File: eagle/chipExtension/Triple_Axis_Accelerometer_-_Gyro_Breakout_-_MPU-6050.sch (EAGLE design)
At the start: 17 parts, among them U1 MPU-6050-1, U3 PCA9685

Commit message: Adding holes to the PCB on eagle and enhancing the freeca model of cylinder prototype 3.
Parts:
- added JP2, JP3, JP4, JP5, JP6, JP7, JP8, JP9: (no value), jumper:JP4E
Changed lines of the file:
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@@
 <part name="P+5" library="supply1" library_urn="urn:adsk.eagle:library:371" deviceset="VCC" device=""/>
 <part name="P+6" library="supply1" library_urn="urn:adsk.eagle:library:371" deviceset="VCC" device=""/>
+<part name="JP2" library="jumper" library_urn="urn:adsk.eagle:library:252" deviceset="JP4E" device=""/>
+<part name="JP3" library="jumper" library_urn="urn:adsk.eagle:library:252" deviceset="JP4E" device=""/>
+<part name="JP4" library="jumper" library_urn="urn:adsk.eagle:library:252" deviceset="JP4E" device=""/>
+<part name="JP5" library="jumper" library_urn="urn:adsk.eagle:library:252" deviceset="JP4E" device=""/>
+<part name="JP6" library="jumper" library_urn="urn:adsk.eagle:library:252" deviceset="JP4E" device=""/>
+<part name="JP7" library="jumper" library_urn="urn:adsk.eagle:library:252" deviceset="JP4E" device=""/>
+<part name="JP8" library="jumper" library_urn="urn:adsk.eagle:library:252" deviceset="JP4E" device=""/>
+<part name="JP9" library="jumper" library_urn="urn:adsk.eagle:library:252" deviceset="JP4E" device=""/>
 </parts>
 <sheets>
@@
 <instance part="P+5" gate="VCC" x="40.64" y="20.32"/>
 <instance part="P+6" gate="VCC" x="40.64" y="10.16"/>
+<instance part="JP2" gate="G$1" x="-177.8" y="93.98" rot="R90"/>
+<instance part="JP3" gate="G$1" x="-177.8" y="76.2" rot="R90"/>
+<instance part="JP4" gate="G$1" x="-177.8" y="55.88" rot="R90"/>
+<instance part="JP5" gate="G$1" x="-177.8" y="35.56" rot="R90"/>
+<instance part="JP6" gate="G$1" x="-193.04" y="96.52" rot="R270"/>
+<instance part="JP7" gate="G$1" x="-193.04" y="78.74" rot="R270"/>
+<instance part="JP8" gate="G$1" x="-193.04" y="58.42" rot="R270"/>
+<instance part="JP9" gate="G$1" x="-193.04" y="38.1" rot="R270"/>
 </instances>
 <busses>

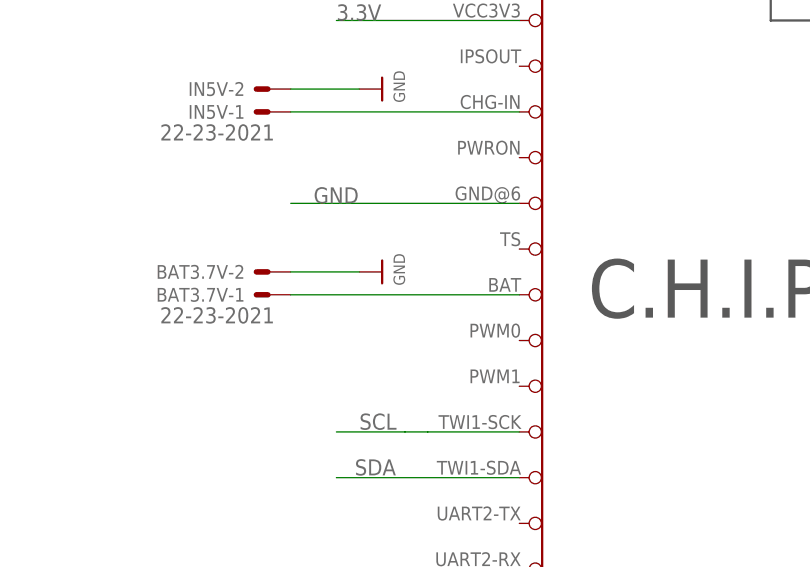
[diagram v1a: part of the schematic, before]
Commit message: Adding jumper to eagle files and enhancing the freecad model of cylinderPrototype3.
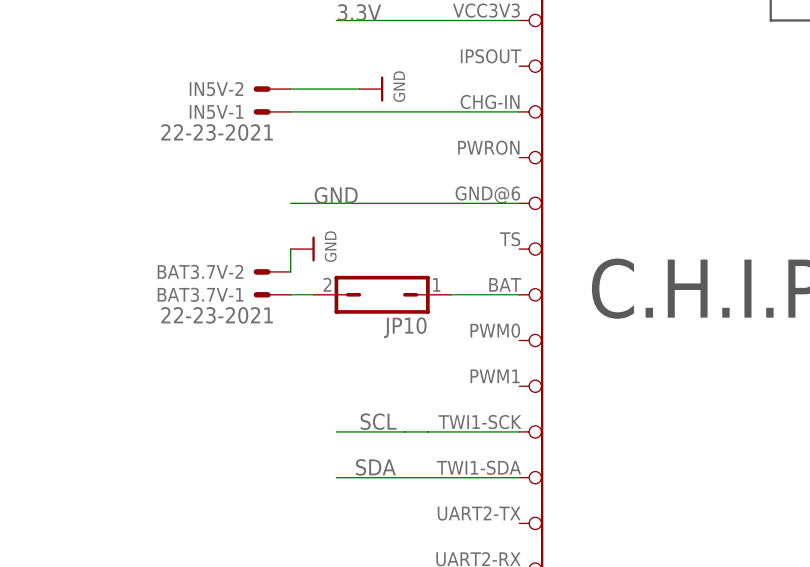
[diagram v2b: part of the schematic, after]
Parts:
- added JP10: (no value), jumper:JP1Q
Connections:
- net VCC: now also JP10.1, JP10.2
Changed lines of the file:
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@@
 <part name="JP8" library="jumper" library_urn="urn:adsk.eagle:library:252" deviceset="JP4E" device=""/>
 <part name="JP9" library="jumper" library_urn="urn:adsk.eagle:library:252" deviceset="JP4E" device=""/>
+<part name="JP10" library="jumper" library_urn="urn:adsk.eagle:library:252" deviceset="JP1Q" device=""/>
 </parts>
 <sheets>
@@
 <instance part="BAT3.7V" gate="-2" x="-144.78" y="71.12" rot="R180"/>
 <instance part="U$2" gate="G$1" x="-132.08" y="91.44" rot="R90"/>
-<instance part="U$3" gate="G$1" x="-132.08" y="71.12" rot="R90"/>
+<instance part="U$3" gate="G$1" x="-139.7" y="73.66" rot="R90"/>
 <instance part="P+3" gate="VCC" x="40.64" y="40.64"/>
 <instance part="P+4" gate="VCC" x="40.64" y="30.48"/>
@@
 <instance part="JP8" gate="G$1" x="-193.04" y="58.42" rot="R270"/>
 <instance part="JP9" gate="G$1" x="-193.04" y="38.1" rot="R270"/>
+<instance part="JP10" gate="A" x="-132.08" y="68.58" rot="R90"/>
 </instances>
 <busses>
@@
 <segment>
 <pinref part="U$1" gate="G$1" pin="BAT"/>
-<pinref part="BAT3.7V" gate="-1" pin="S"/>
-<wire x1="-142.24" y1="68.58" x2="-116.84" y2="68.58" width="0.1524" layer="91"/>
+<pinref part="JP10" gate="A" pin="1"/>
+<wire x1="-124.46" y1="68.58" x2="-116.84" y2="68.58" width="0.1524" layer="91"/>
 </segment>
 <segment>
@@
 <pinref part="JP1" gate="G$1" pin="11"/>
 <pinref part="P+6" gate="VCC" pin="VCC"/>
+</segment>
+<segment>
+<pinref part="BAT3.7V" gate="-1" pin="S"/>
+<wire x1="-142.24" y1="68.58" x2="-139.7" y2="68.58" width="0.1524" layer="91"/>
+<pinref part="JP10" gate="A" pin="2"/>
 </segment>
 </net>
@@
 <segment>
 <pinref part="BAT3.7V" gate="-2" pin="S"/>
-<wire x1="-142.24" y1="71.12" x2="-134.62" y2="71.12" width="0.1524" layer="91"/>
+<wire x1="-142.24" y1="71.12" x2="-142.24" y2="73.66" width="0.1524" layer="91"/>
 <pinref part="U$3" gate="G$1" pin="GND"/>
 </segment>

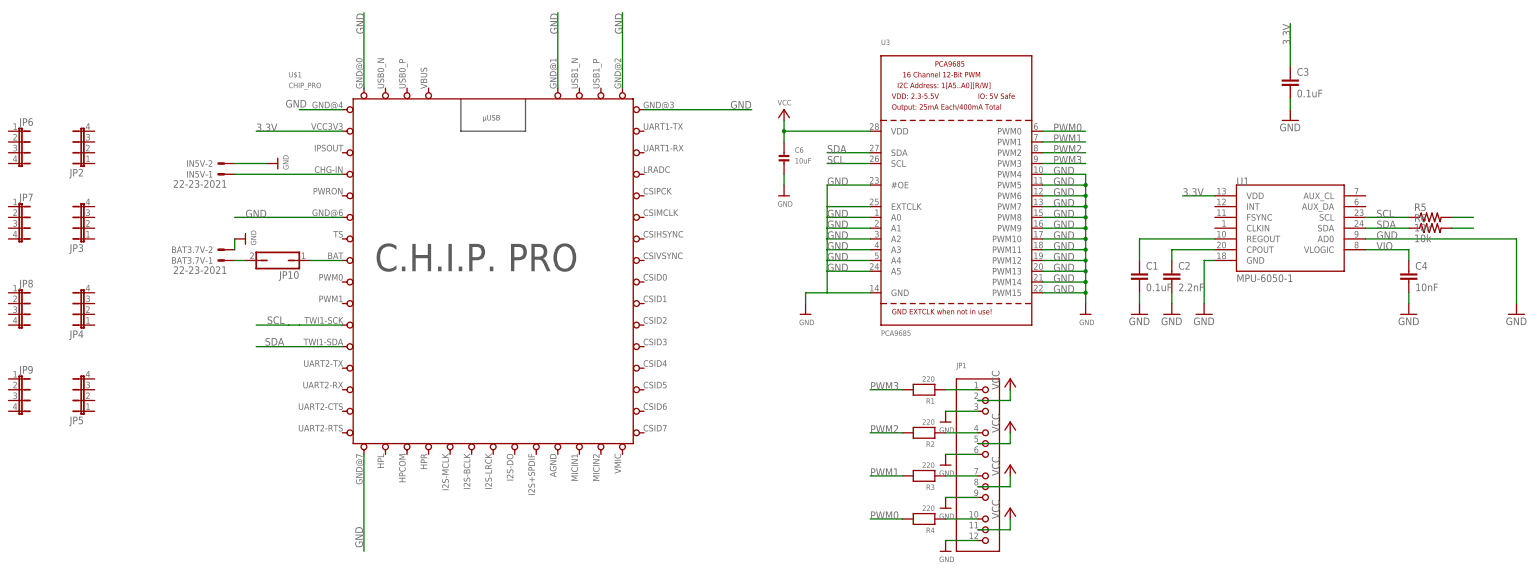
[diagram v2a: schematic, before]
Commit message: improve eagle design
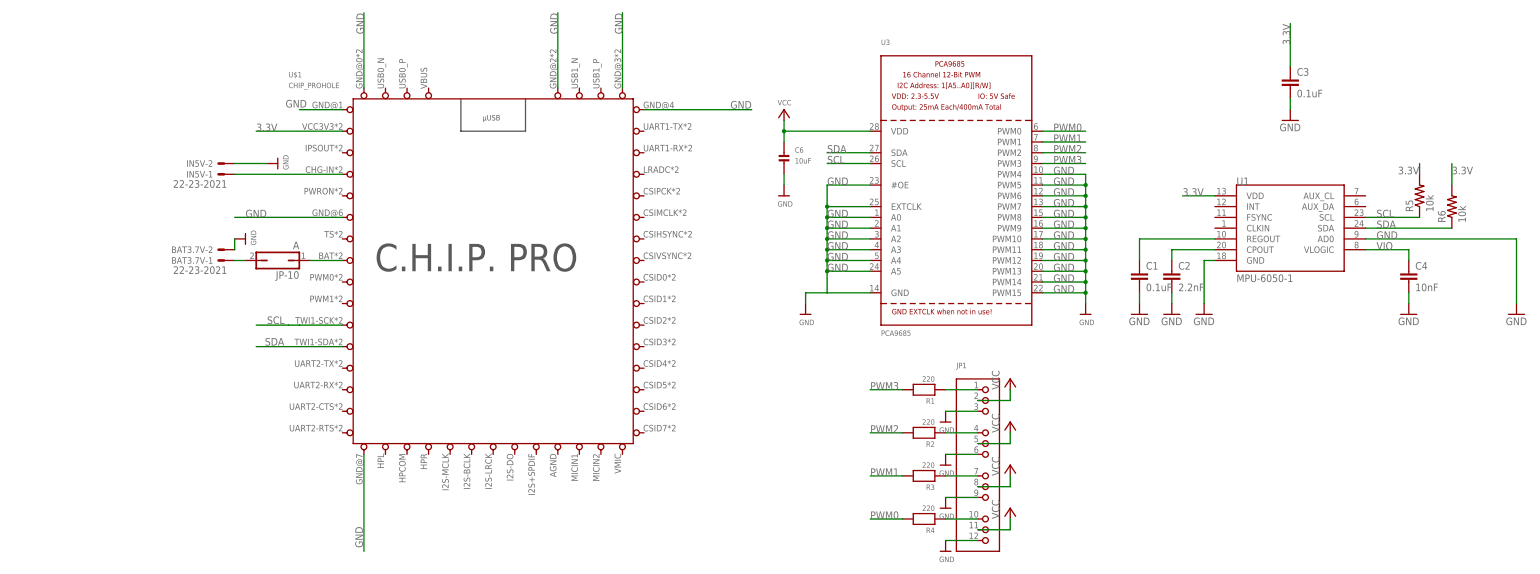
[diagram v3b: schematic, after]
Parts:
- removed JP2, JP3, JP4, JP5, JP6, JP7, JP8, JP9: (no value), jumper:JP4E
- JP-10: value (none) -> A
- U$1: value CHIP_PRO -> CHIP_PROHOLE; device CHIP_Pro-Footprint:CHIP_PRO -> CHIP_Pro-Footprint:CHIP_PROHOLE
- renumbered JP10 to JP-10
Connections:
- net 3.3V: now also R5.2, R6.2
- net SCL: no longer R5.2
- net SDA: no longer R6.2
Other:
- moved on the sheet: R5, R6, U$1
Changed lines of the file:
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@@
 <part name="R4" library="microbuilder" deviceset="RESISTOR" device="0805" value="220"/>
 <part name="JP1" library="microbuilder" deviceset="HEADER-3X04" device=""/>
-<part name="U$1" library="CHIP_Pro-Footprint" deviceset="CHIP_PRO" device=""/>
+<part name="U$1" library="CHIP_Pro-Footprint" deviceset="CHIP_PRO" device="HOLE" value="CHIP_PROHOLE"/>
 <part name="U$9" library="microbuilder" deviceset="GND" device=""/>
 <part name="R5" library="rcl" library_urn="urn:adsk.eagle:library:334" deviceset="R-US_" device="R0805" value="10k"/>
@@
 <part name="P+5" library="supply1" library_urn="urn:adsk.eagle:library:371" deviceset="VCC" device=""/>
 <part name="P+6" library="supply1" library_urn="urn:adsk.eagle:library:371" deviceset="VCC" device=""/>
-<part name="JP2" library="jumper" library_urn="urn:adsk.eagle:library:252" deviceset="JP4E" device=""/>
-<part name="JP3" library="jumper" library_urn="urn:adsk.eagle:library:252" deviceset="JP4E" device=""/>
-<part name="JP4" library="jumper" library_urn="urn:adsk.eagle:library:252" deviceset="JP4E" device=""/>
-<part name="JP5" library="jumper" library_urn="urn:adsk.eagle:library:252" deviceset="JP4E" device=""/>
-<part name="JP6" library="jumper" library_urn="urn:adsk.eagle:library:252" deviceset="JP4E" device=""/>
-<part name="JP7" library="jumper" library_urn="urn:adsk.eagle:library:252" deviceset="JP4E" device=""/>
-<part name="JP8" library="jumper" library_urn="urn:adsk.eagle:library:252" deviceset="JP4E" device=""/>
-<part name="JP9" library="jumper" library_urn="urn:adsk.eagle:library:252" deviceset="JP4E" device=""/>
-<part name="JP10" library="jumper" library_urn="urn:adsk.eagle:library:252" deviceset="JP1Q" device=""/>
+<part name="JP-10" library="jumper" library_urn="urn:adsk.eagle:library:252" deviceset="JP1Q" device="" value="A"/>
 </parts>
 <sheets>
@@
 <instance part="U$1" gate="G$1" x="-81.28" y="63.5"/>
 <instance part="U$9" gate="G$1" x="58.42" y="55.88"/>
-<instance part="R5" gate="G$1" x="139.7" y="78.74"/>
-<instance part="R6" gate="G$1" x="139.7" y="76.2"/>
+<instance part="R5" gate="G$1" x="137.16" y="83.82" rot="R90"/>
+<instance part="R6" gate="G$1" x="144.78" y="81.28" rot="R90"/>
 <instance part="IN5V" gate="-1" x="-144.78" y="88.9" rot="R180"/>
 <instance part="IN5V" gate="-2" x="-144.78" y="91.44" rot="R180"/>
@@
 <instance part="P+5" gate="VCC" x="40.64" y="20.32"/>
 <instance part="P+6" gate="VCC" x="40.64" y="10.16"/>
-<instance part="JP2" gate="G$1" x="-177.8" y="93.98" rot="R90"/>
-<instance part="JP3" gate="G$1" x="-177.8" y="76.2" rot="R90"/>
-<instance part="JP4" gate="G$1" x="-177.8" y="55.88" rot="R90"/>
-<instance part="JP5" gate="G$1" x="-177.8" y="35.56" rot="R90"/>
-<instance part="JP6" gate="G$1" x="-193.04" y="96.52" rot="R270"/>
-<instance part="JP7" gate="G$1" x="-193.04" y="78.74" rot="R270"/>
-<instance part="JP8" gate="G$1" x="-193.04" y="58.42" rot="R270"/>
-<instance part="JP9" gate="G$1" x="-193.04" y="38.1" rot="R270"/>
-<instance part="JP10" gate="A" x="-132.08" y="68.58" rot="R90"/>
+<instance part="JP-10" gate="A" x="-132.08" y="68.58" rot="R90"/>
 </instances>
 <busses>
@@
 <segment>
 <pinref part="U$1" gate="G$1" pin="BAT"/>
-<pinref part="JP10" gate="A" pin="1"/>
+<pinref part="JP-10" gate="A" pin="1"/>
 <wire x1="-124.46" y1="68.58" x2="-116.84" y2="68.58" width="0.1524" layer="91"/>
 </segment>
@@
 <pinref part="BAT3.7V" gate="-1" pin="S"/>
 <wire x1="-142.24" y1="68.58" x2="-139.7" y2="68.58" width="0.1524" layer="91"/>
-<pinref part="JP10" gate="A" pin="2"/>
+<pinref part="JP-10" gate="A" pin="2"/>
 </segment>
 </net>
@@
 <pinref part="U3" gate="G$1" pin="#OE"/>
 <wire x1="-2.54" y1="86.36" x2="-2.54" y2="81.28" width="0.1524" layer="91"/>
+<junction x="-2.54" y="81.28"/>
+<junction x="-2.54" y="78.74"/>
+<junction x="-2.54" y="76.2"/>
+<junction x="-2.54" y="73.66"/>
+<junction x="-2.54" y="71.12"/>
+<junction x="-2.54" y="68.58"/>
+<junction x="-2.54" y="66.04"/>
 </segment>
 <segment>
@@
 <pinref part="U1" gate="G$1" pin="SCL"/>
 <pinref part="R5" gate="G$1" pin="1"/>
-<wire x1="134.62" y1="78.74" x2="124.46" y2="78.74" width="0.1524" layer="91"/>
+<wire x1="137.16" y1="78.74" x2="124.46" y2="78.74" width="0.1524" layer="91"/>
 </segment>
 <segment>
@@
 <label x="-134.62" y="53.594" size="1.778" layer="95"/>
 </segment>
-<segment>
-<pinref part="R5" gate="G$1" pin="2"/>
-<wire x1="144.78" y1="78.74" x2="149.86" y2="78.74" width="0.1524" layer="91"/>
-</segment>
 </net>
 <net name="SDA" class="0">
@@
 <pinref part="U1" gate="G$1" pin="SDA"/>
 <pinref part="R6" gate="G$1" pin="1"/>
-<wire x1="134.62" y1="76.2" x2="124.46" y2="76.2" width="0.1524" layer="91"/>
+<wire x1="144.78" y1="76.2" x2="124.46" y2="76.2" width="0.1524" layer="91"/>
 </segment>
 <segment>
@@
 <wire x1="-116.84" y1="48.26" x2="-137.16" y2="48.26" width="0.1524" layer="91"/>
 <label x="-135.128" y="48.514" size="1.778" layer="95"/>
-</segment>
-<segment>
-<pinref part="R6" gate="G$1" pin="2"/>
-<wire x1="144.78" y1="76.2" x2="149.86" y2="76.2" width="0.1524" layer="91"/>
 </segment>
 </net>
@@
 <label x="106.68" y="119.38" size="1.778" layer="95" rot="R90"/>
 </segment>
+<segment>
+<pinref part="R5" gate="G$1" pin="2"/>
+<wire x1="137.16" y1="88.9" x2="137.16" y2="91.44" width="0.1524" layer="91"/>
+<label x="132.08" y="88.9" size="1.778" layer="95"/>
+</segment>
+<segment>
+<pinref part="R6" gate="G$1" pin="2"/>
+<wire x1="144.78" y1="86.36" x2="144.78" y2="91.44" width="0.1524" layer="91"/>
+<label x="144.78" y="88.9" size="1.778" layer="95"/>
+</segment>
 </net>
 </nets>
 </sheet>
 </sheets>
-<errors>
-</errors>
 </schematic>
 </drawing>
